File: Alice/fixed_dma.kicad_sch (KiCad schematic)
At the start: 153 parts, among them Q285 NOT_OC, Q286 NOT_OC, Q287 NOT_OC, Q288 NOT_OC, Q289 NOT_OC, Q290 NOT_OC, Q291 NOT_OC, Q292 NOT_OC, Q293 NOT_OC, Q294 NOT_OC, Q295 NOT_OC, Q296 NOT_OC, Q297 NOT_OC, Q298 NOT_OC, Q299 NOT_OC, Q300 NOT_OC, Q301 NOT_OC, Q302 NOT_OC, Q303 NOT_OC, Q304 NOT_OC, Q305 NOT_OC, Q306 NOT_OC, Q307 NOT_OC, Q308 NOT_OC, Q309 NOT_OC, Q310 NOT_OC, Q311 NOT_OC, Q312 NOT_OC, Q313 NOT_OC, Q314 NOT_OC, Q315 NOT_OC, Q316 NOT_OC, Q317 NOT_OC, Q318 NOT_OC, Q319 NOT_OC, Q320 NOT_OC, Q321 NOT_OC, Q322 NOT_OC, Q323 NOT_OC, Q324 NOT_OC, Q325 NOT_OC, Q326 NOT_OC, Q327 NOT_OC, Q328 NOT_OC, Q329 NOT_OC, Q330 NOT_OC, Q331 NOT_OC, Q332 NOT_OC

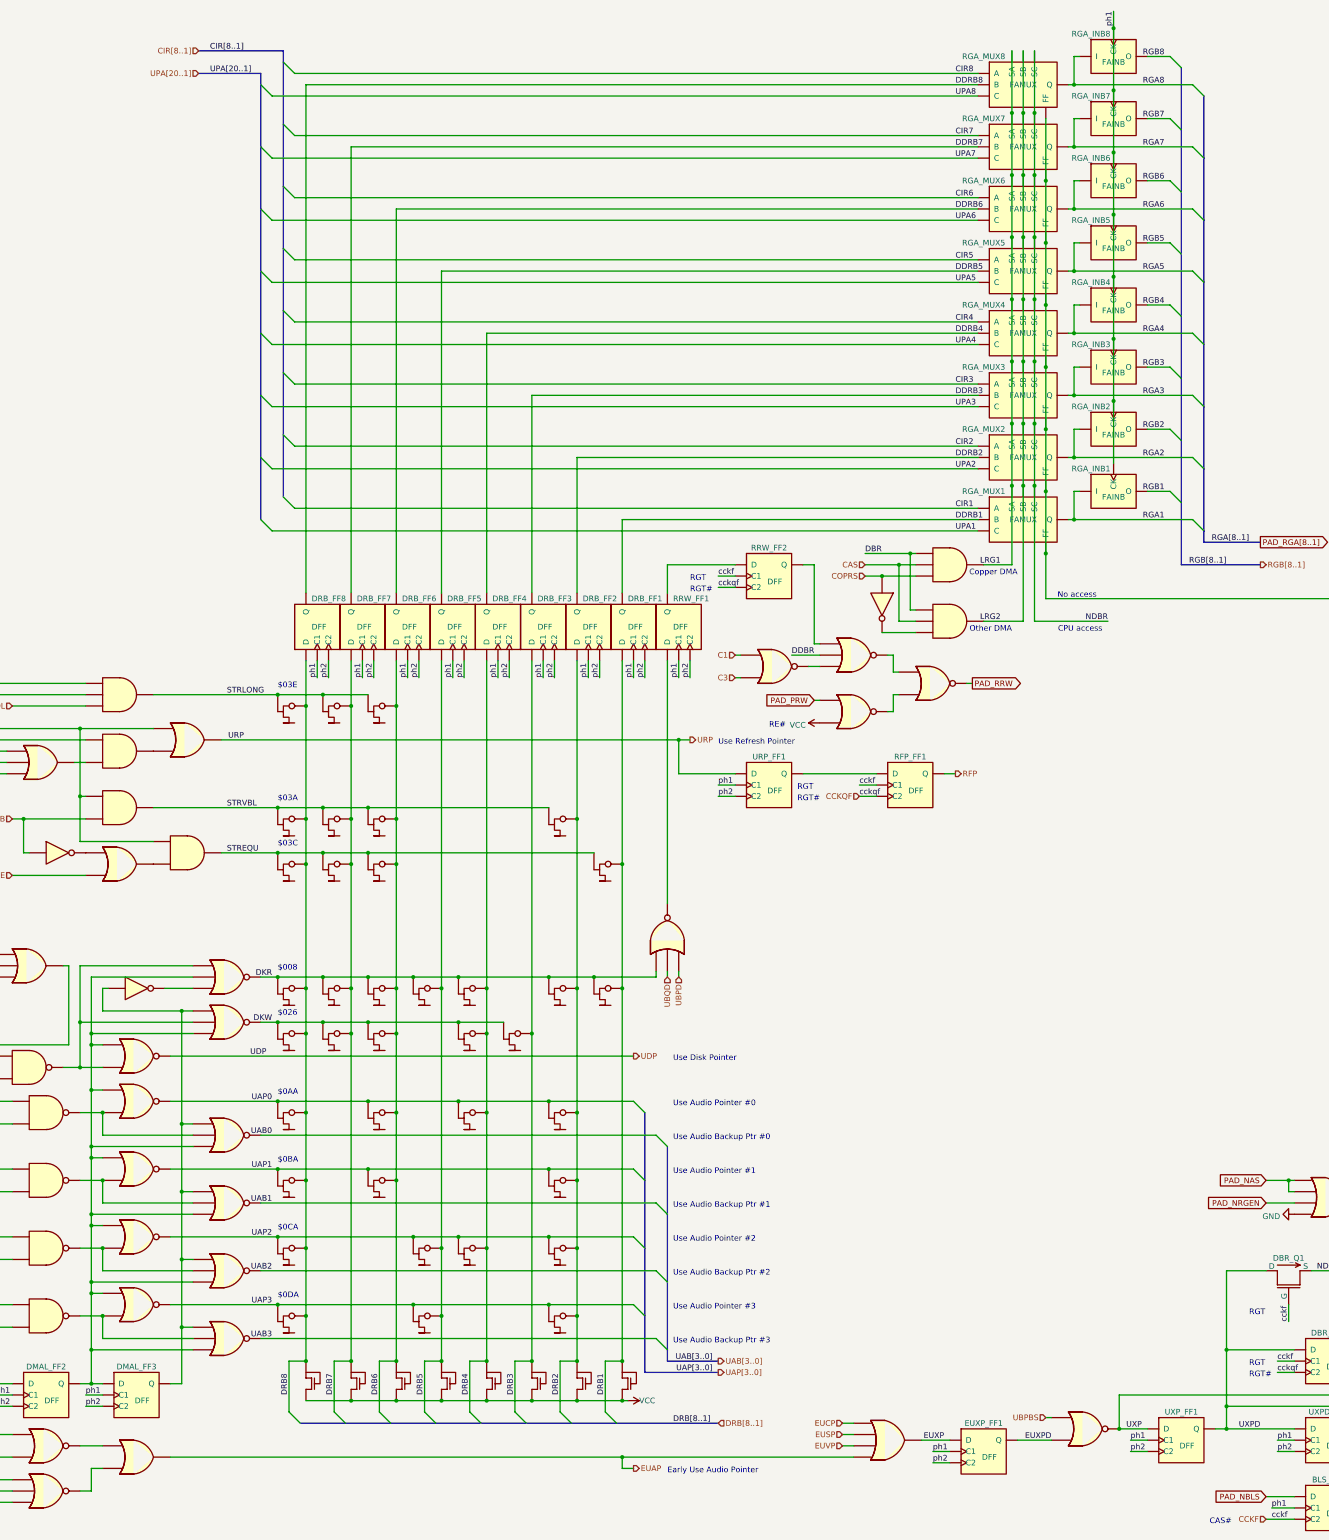
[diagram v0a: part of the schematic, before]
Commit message: Added Copper DMA schematics (WIP)
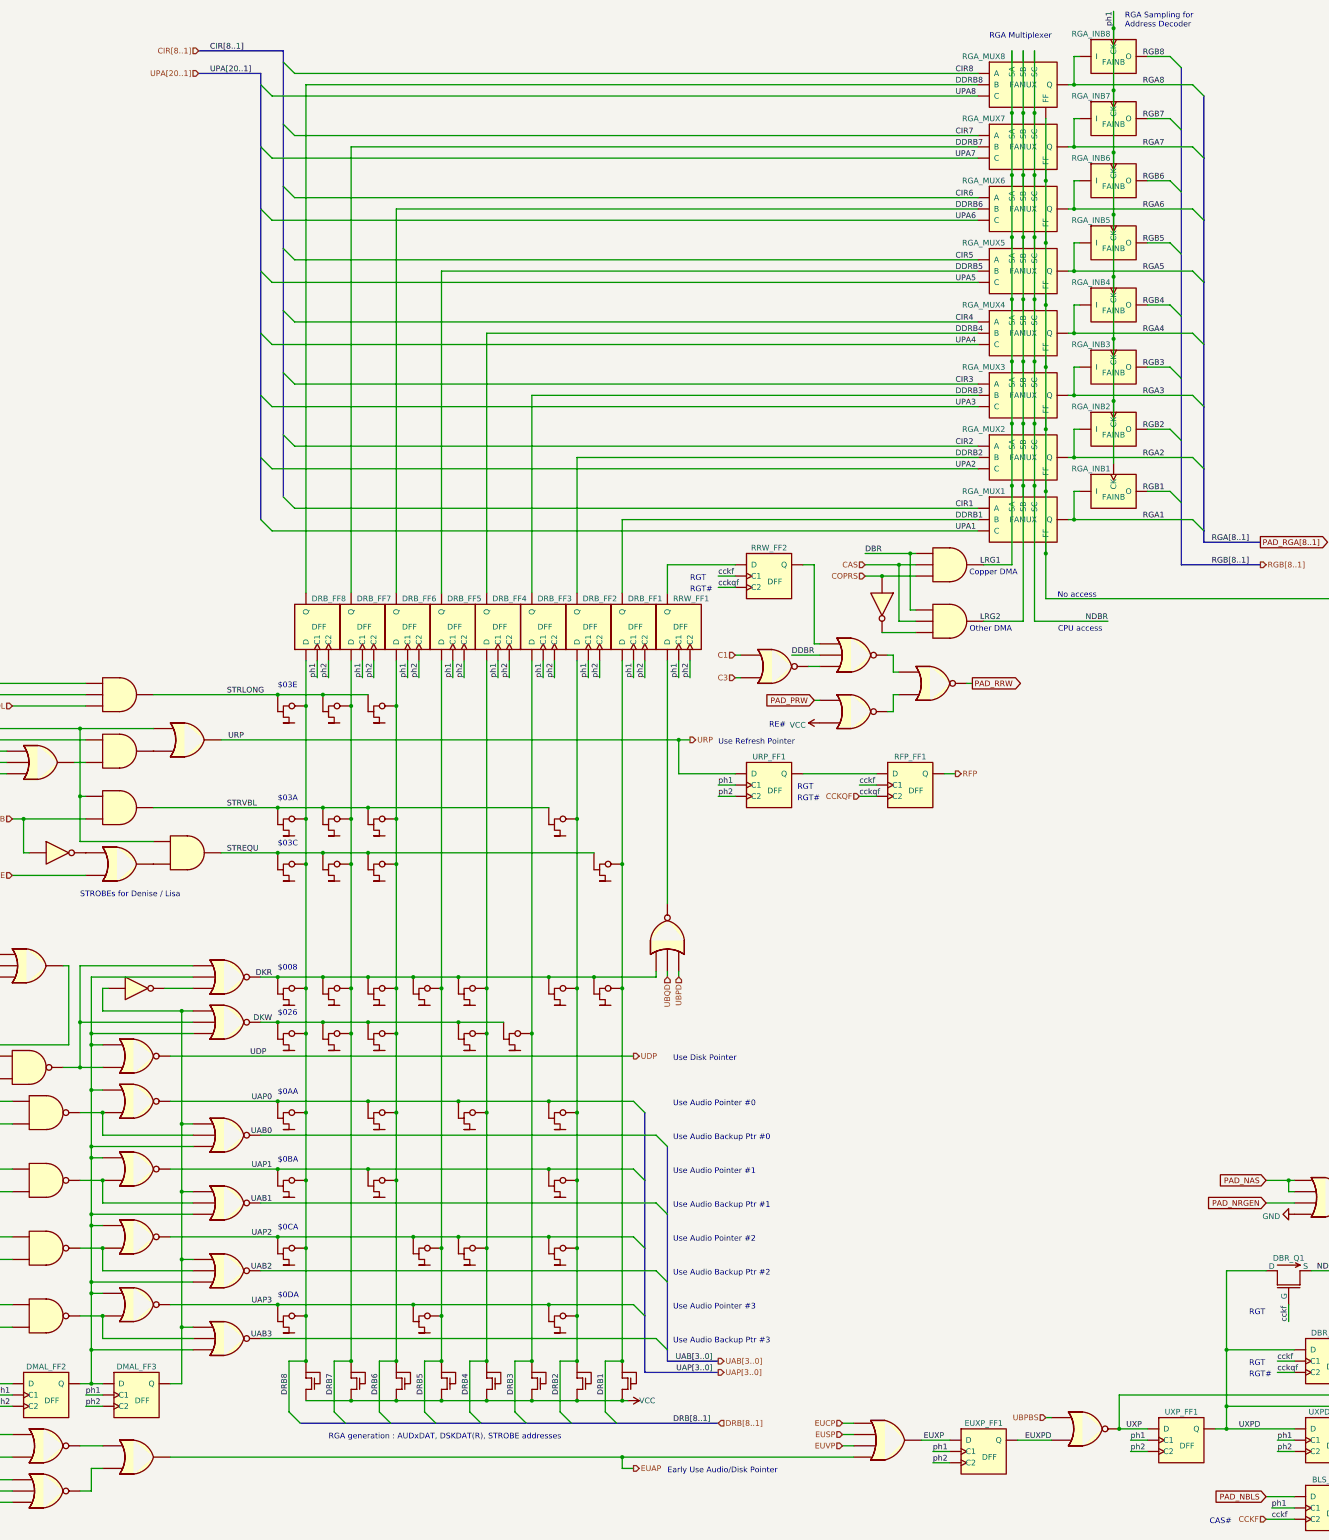
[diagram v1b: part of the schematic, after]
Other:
- note added: "Early Use Audio/Disk Pointer"
- note added: "RGA Multiplexer"
- note added: "RGA Sampling for Address Decoder"
- note added: "RGA generation : AUDxDAT, DSKDAT(R), STROBE addresses"
- note added: "STROBEs for Denise / Lisa"
- note removed: "Early Use Audio Pointer"
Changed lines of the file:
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@@
+    (effects (font (size 1.27 1.27)) (justify left bottom))
+  )
+  (text "RGA generation : AUDxDAT, DSKDAT(R), STROBE addresses"
+    (at 168.91 336.55 0)
     (effects (font (size 1.27 1.27)) (justify left bottom))
   )
@@
     (effects (font (size 1.27 1.27)) (justify left bottom))
   )
+  (text "RGA Sampling for\nAddress Decoder" (at 347.98 19.05 0)
+    (effects (font (size 1.27 1.27)) (justify left bottom))
+  )
   (text "Audio #1" (at 45.72 279.4 0)
     (effects (font (size 1.27 1.27)) (justify left bottom))
@@
     (effects (font (size 1.27 1.27)) (justify left bottom))
   )
-  (text "Early Use Audio Pointer" (at 245.11 344.17 0)
+  (text "Early Use Audio/Disk Pointer" (at 245.11 344.17 0)
     (effects (font (size 1.27 1.27)) (justify left bottom))
   )
@@
     (effects (font (size 1.27 1.27)) (justify left bottom))
   )
+  (text "STROBEs for Denise / Lisa" (at 113.03 214.63 0)
+    (effects (font (size 1.27 1.27)) (justify left bottom))
+  )
   (text "Use Audio Pointer #0" (at 246.38 261.62 0)
     (effects (font (size 1.27 1.27)) (justify left bottom))
@@
     (effects (font (size 1.27 1.27)) (justify left bottom))
   )
+  (text "RGA Multiplexer" (at 317.5 21.59 0)
+    (effects (font (size 1.27 1.27)) (justify left bottom))
+  )
   (text "Disk" (at 45.72 248.92 0)
     (effects (font (size 1.27 1.27)) (justify left bottom))
@@
     (effects (font (size 1.27 1.27)) (justify left bottom))
   )
-  (label "RGB[8..1]" (at 370.84 139.7 180)
-    (effects (font (size 1.27 1.27)) (justify right bottom))
-  )
+  (label "RGB[8..1]" (at 375.92 139.7 180)
+    (effects (font (size 1.27 1.27)) (justify right bottom))
+  )

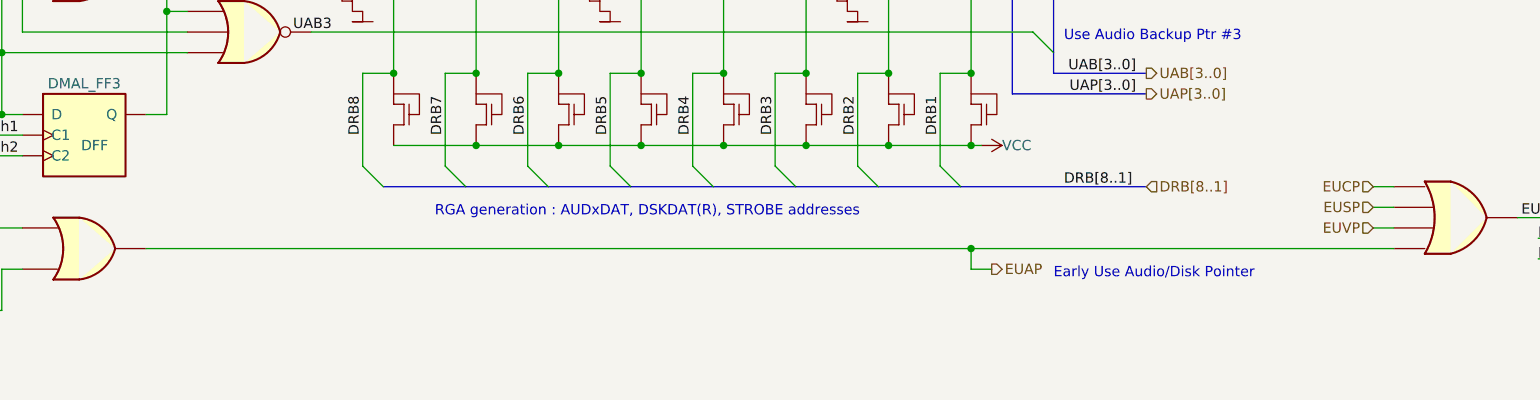
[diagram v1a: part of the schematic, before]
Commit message: Preparing DMA pointers sheet
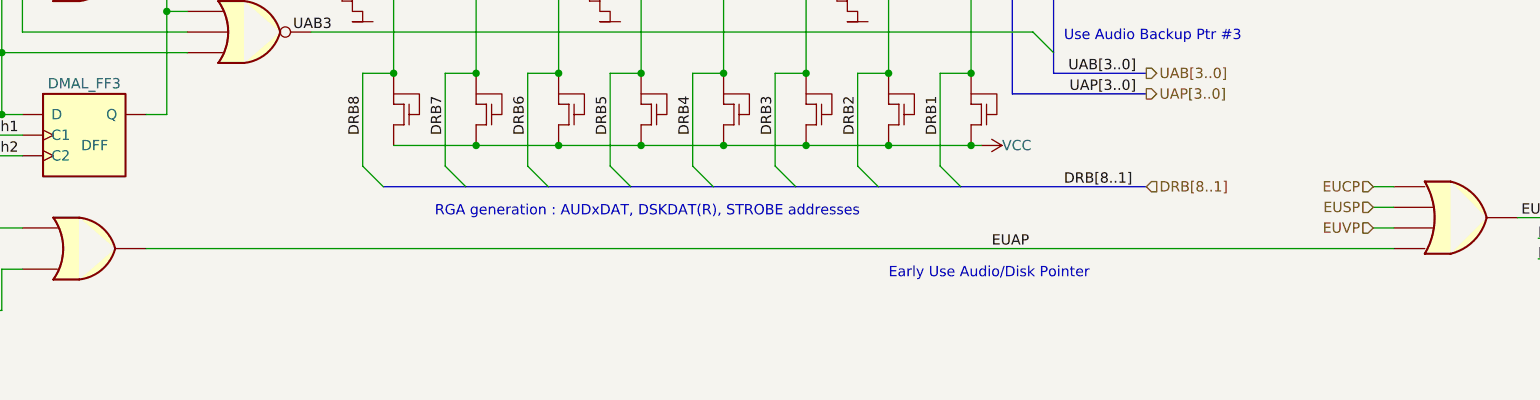
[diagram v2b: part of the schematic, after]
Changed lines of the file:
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@@
   (junction (at 85.09 201.93) (diameter 0) (color 0 0 0 0)
   )
-  (junction (at 234.95 340.36) (diameter 0) (color 0 0 0 0)
-  )
   (junction (at 198.12 232.41) (diameter 0) (color 0 0 0 0)
   )
@@
     (stroke (width 0) (type default) (color 0 0 0 0))
   )
-  (wire (pts (xy 234.95 340.36) (xy 287.02 340.36))
+  (wire (pts (xy 133.35 340.36) (xy 287.02 340.36))
     (stroke (width 0) (type default) (color 0 0 0 0))
   )
@@
     (stroke (width 0) (type default) (color 0 0 0 0))
   )
-  (wire (pts (xy 234.95 342.9) (xy 237.49 342.9))
-    (stroke (width 0) (type default) (color 0 0 0 0))
-  )
   (wire (pts (xy 78.74 194.31) (xy 78.74 184.15))
     (stroke (width 0) (type default) (color 0 0 0 0))
@@
     (stroke (width 0) (type default) (color 0 0 0 0))
   )
-  (wire (pts (xy 234.95 340.36) (xy 234.95 342.9))
-    (stroke (width 0) (type default) (color 0 0 0 0))
-  )
   (wire (pts (xy 153.67 298.45) (xy 242.57 298.45))
     (stroke (width 0) (type default) (color 0 0 0 0))
@@
   )
   (wire (pts (xy 198.12 242.57) (xy 208.28 242.57))
-    (stroke (width 0) (type default) (color 0 0 0 0))
-  )
-  (wire (pts (xy 133.35 340.36) (xy 234.95 340.36))
     (stroke (width 0) (type default) (color 0 0 0 0))
   )
@@
     (effects (font (size 1.27 1.27)) (justify left bottom))
   )
-  (text "Early Use Audio/Disk Pointer" (at 245.11 344.17 0)
+  (text "Early Use Audio/Disk Pointer" (at 224.79 344.17 0)
     (effects (font (size 1.27 1.27)) (justify left bottom))
   )
@@
   )
   (text "Refresh" (at 45.72 167.64 0)
+    (effects (font (size 1.27 1.27)) (justify left bottom))
+  )
+  (label "EUAP" (at 237.49 340.36 0)
     (effects (font (size 1.27 1.27)) (justify left bottom))
   )
@@
     (effects (font (size 1.27 1.27)) (justify left))
   )
-  (hierarchical_label "EUAP" (shape output) (at 237.49 342.9 0)
-    (effects (font (size 1.27 1.27)) (justify left))
-  )
